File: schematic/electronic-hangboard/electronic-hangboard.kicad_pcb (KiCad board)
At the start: 2 copper layers, 74 x 45.3 mm, 40 parts, among them J1 UART, J2 Load cell, J3 JTAG, J4 Battery, Q1 2N7002, SW1 RESET, SW2 POWER_ON, U1 ESP32-WROOM-32, U2 HX711, U3 NCP1400A, U4 AMS1117-3.3

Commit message: Update pcb
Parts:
- removed C10: 68uF, Capacitor_SMD:C_1206_3216Metric_Pad1.33x1.80mm_HandSolder
- removed C9: 10uF, Capacitor_SMD:C_1206_3216Metric_Pad1.33x1.80mm_HandSolder
- removed H2, H3: MountingHole, MountingHole:MountingHole_3.2mm_M3
- removed L1: CR54−220MC - 22uH, Inductor_SMD:L_Bourns_SRP7028A_7.3x6.6mm
- removed SW1: RESET, Button_Switch_SMD:SW_Push_1P1T_NO_6x6mm_H9.5mm
- removed SW2: POWER_ON, Button_Switch_SMD:SW_Push_1P1T_NO_6x6mm_H9.5mm
- removed U3: NCP1400A, Package_TO_SOT_SMD:SOT-23-5_HandSoldering
- added C13: 4.7uF, Capacitor_SMD:C_1206_3216Metric_Pad1.33x1.80mm_HandSolder, F.Cu at (61.0, 65.2)
- added C14: 3.3pF, Capacitor_SMD:C_1206_3216Metric_Pad1.33x1.80mm_HandSolder, F.Cu at (49.5, 70.3)
- added C15: 4.7uF, Capacitor_SMD:C_1206_3216Metric_Pad1.33x1.80mm_HandSolder, F.Cu at (49.5, 65.2)
- added D2: MBR0520LT1, Diode_SMD:D_SOD-123, F.Cu at (49.8, 58.9)
- added D3: LED, Diode_SMD:D_1206_3216Metric_Pad1.42x1.75mm_HandSolder, F.Cu at (81.0, 36.1)
- added J5: UART, Connector_PinHeader_2.54mm:PinHeader_1x06_P2.54mm_Vertical, F.Cu at (34.3, 53.3)
- added J6: Conn_01x10_Pin, Connector_PinHeader_2.54mm:PinHeader_1x10_P2.54mm_Vertical, F.Cu at (72.6, 65.0)
- added L2: 10uH, Inductor_SMD:L_Bourns_SRP7028A_7.3x6.6mm, F.Cu at (57.1, 58.9)
- added R13: 200K, Resistor_SMD:R_1206_3216Metric_Pad1.30x1.75mm_HandSolder, F.Cu at (57.1, 67.8)
- added R14: 10K, Resistor_SMD:R_1206_3216Metric_Pad1.30x1.75mm_HandSolder, F.Cu at (59.4, 70.3)
- added R15: 330R, Resistor_SMD:R_1206_3216Metric_Pad1.30x1.75mm_HandSolder, F.Cu at (91.9, 36.1)
- added SW3: POWER_ON, Connector_PinHeader_2.54mm:PinHeader_1x02_P2.54mm_Vertical_SMD_Pin1Left, F.Cu at (66.0, 58.4)
- added U5: TPS61040DBV, Package_TO_SOT_SMD:SOT-23-5, F.Cu at (56.9, 64.5)
- D1: value MBR0520LT1 -> LED; footprint Diode_SMD:D_SOD-123 -> Diode_SMD:D_1206_3216Metric_Pad1.42x1.75mm_HandSolder
- H1: footprint MountingHole:MountingHole_3.2mm_M3 -> MountingHole:MountingHole_3.2mm_M3_DIN965_Pad_TopBottom
- J1: value UART -> BATTERY; footprint Connector_PinHeader_2.54mm:PinHeader_1x03_P2.54mm_Vertical -> Connector_PinHeader_2.54mm:PinHeader_1x02_P2.54mm_Vertical
- J2: value Load cell -> Conn_01x04_Pin; footprint Connector_Wire:SolderWire-0.1sqmm_1x04_P3.6mm_D0.4mm_OD1mm_Relief -> Connector_PinHeader_2.54mm:PinHeader_1x04_P2.54mm_Vertical
- J3: footprint Connector_PinHeader_2.54mm:PinHeader_1x07_P2.54mm_Vertical -> Connector_PinHeader_2.54mm:PinHeader_1x06_P2.54mm_Vertical
- J4: value Battery -> Conn_01x10_Pin; footprint Connector_Wire:SolderWire-0.1sqmm_1x02_P3.6mm_D0.4mm_OD1mm -> Connector_PinHeader_2.54mm:PinHeader_1x10_P2.54mm_Vertical
- Q1: value 2N7002 -> S9015
- R1: value R -> 10K
- R12: value 10K -> 330R
- R8: value 100R -> 620K
- R9: value 100R -> 1K2
- moved R8 131.4 mm to (49.5, 67.8), turned to 0 degrees
- moved U4 128.2 mm to (42.4, 60.3), turned to 90 degrees
- moved J1 126.9 mm to (34.3, 70.9), turned to 0 degrees
- moved C11 120.3 mm to (42.4, 67.5), turned to 90 degrees
- moved R2 110.8 mm to (38.9, 40.6)
- moved R3 110.8 mm to (38.8, 43.2)
- moved R5 110.7 mm to (38.8, 48.3)
- moved R4 110.7 mm to (38.9, 45.7)
- moved D1 110.2 mm to (75.4, 36.1), turned to 180 degrees
- moved R12 109.7 mm to (86.6, 36.1), turned to 180 degrees
- moved J3 108.5 mm to (34.3, 35.6)
- moved C3 105.4 mm to (37.8, 36.3)
- moved C6 103.7 mm to (91.8, 47.0)
- moved J2 103.4 mm to (95.6, 48.5), turned to 180 degrees
- moved R7 102.1 mm to (90.2, 41.6)
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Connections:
- C1 pad 2: GND -> E-
- C11 pad 1: GND -> E-
- C12 pad 2: GND -> E-
- C2 pad 2: GND -> E-
- C3 pad 1: GND -> E-
- C4 pad 2: GND -> E-
- C5 pad 1: GND -> E-
- C6 pad 1: GND -> E-
- C6 pad 2: Net-(J2-Pin_1) -> E+
- C7 pad 2: Net-(U2-INA-) -> S-
- D1 pad 1: +5V -> Net-(D1-K)
- D1 pad 2: Net-(D1-A) -> IO23
- J1 pad 1: TX -> E-
- J1 pad 2: RX -> +BATT
- J2 pad 1: Net-(J2-Pin_1) -> E+
- J2 pad 2: GND -> E-
- J2 pad 3: S- -> S+
- J2 pad 4: S+ -> S-
- J3 pad 2: GND -> E-
- J3 pad 3: EN -> Net-(J3-Pin_3)
- J3 pad 4: Net-(J3-TCK) -> Net-(J3-Pin_4)
- J3 pad 5: Net-(J3-TMS) -> Net-(J3-Pin_5)
- J3 pad 6: Net-(J3-TDO) -> Net-(J3-Pin_6)
- J4 pad 1: +BATT -> IO2
- J4 pad 2: GND -> SDI
- Q1 pad 1: Net-(Q1-G) -> E+
- Q1 pad 2: Net-(J2-Pin_1) -> Net-(Q1-B)
- R11 pad 2: GND -> E-
- R12 pad 1: CONV_EN -> E-
- R12 pad 2: GND -> Net-(D1-K)
- R2 pad 1: Net-(J3-TCK) -> Net-(J3-Pin_3)
- R3 pad 1: Net-(J3-TMS) -> Net-(J3-Pin_4)
- R4 pad 1: Net-(J3-TDO) -> Net-(J3-Pin_5)
- R5 pad 1: Net-(J3-TDI) -> Net-(J3-Pin_6)
- R6 pad 1: Net-(J2-Pin_1) -> E+
- R7 pad 2: GND -> E-
- R8 pad 1: S- -> +5V
- R8 pad 2: Net-(U2-INA-) -> Net-(U5-FB)
- U1 pad 1: GND -> E-
- U1 pad 10: unconnected-(U1-IO25-Pad10) -> IO25
- U1 pad 11: unconnected-(U1-IO26-Pad11) -> IO26
- U1 pad 12: unconnected-(U1-IO27-Pad12) -> IO27
- U1 pad 15: GND -> E-
- U1 pad 17: unconnected-(U1-SHD/SD2-Pad17) -> SHD
- U1 pad 18: unconnected-(U1-SWP/SD3-Pad18) -> SWP
- U1 pad 19: unconnected-(U1-SCS/CMD-Pad19) -> SCS
- U1 pad 20: unconnected-(U1-SCK/CLK-Pad20) -> SCK
- U1 pad 21: unconnected-(U1-SDO/SD0-Pad21) -> SDO
- U1 pad 22: unconnected-(U1-SDI/SD1-Pad22) -> SDI
- U1 pad 24: unconnected-(U1-IO2-Pad24) -> IO2
- U1 pad 25: Net-(SW1-A) -> RST
- U1 pad 31: SCK -> HX711_SCK
- U1 pad 33: unconnected-(U1-IO21-Pad33) -> IO21
- U1 pad 36: unconnected-(U1-IO22-Pad36) -> IO22
- U1 pad 37: unconnected-(U1-IO23-Pad37) -> IO23
- U1 pad 38: GND -> E-
- U1 pad 39: GND -> E-
- U1 pad 4: unconnected-(U1-SENSOR_VP-Pad4) -> VP
- U1 pad 5: unconnected-(U1-SENSOR_VN-Pad5) -> VN
- U1 pad 6: unconnected-(U1-IO34-Pad6) -> IO34
- U1 pad 7: unconnected-(U1-IO35-Pad7) -> IO35
- U1 pad 8: unconnected-(U1-IO32-Pad8) -> IO32
- U1 pad 9: unconnected-(U1-IO33-Pad9) -> IO33
- U2 pad 10: GND -> E-
- U2 pad 11: SCK -> HX711_SCK
- U2 pad 13: GND -> E-
- U2 pad 2: Net-(Q1-G) -> Net-(Q1-B)
- U2 pad 3: Net-(J2-Pin_1) -> E+
- U2 pad 5: GND -> E-
- U2 pad 7: Net-(U2-INA-) -> S-
- U2 pad 9: GND -> E-
- U4 pad 1: GND -> E-
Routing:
- net E-: track 0.00 -> 170.1 mm, vias 0 -> 2
- net GND: track 158.7 -> 0.00 mm
- net IO25: track 0.00 -> 79.6 mm, vias 0 -> 1
- net IO26: track 0.00 -> 76.3 mm, vias 0 -> 1
- net IO27: track 0.00 -> 73.9 mm, vias 0 -> 1
- net SHD: track 0.00 -> 67.7 mm, vias 0 -> 1
- net SWP: track 0.00 -> 63.4 mm, vias 0 -> 1
- net SCS: track 0.00 -> 60.0 mm, vias 0 -> 1
- net IO22: track 0.00 -> 55.6 mm, vias 0 -> 3
- net VP: track 0.00 -> 54.1 mm, vias 0 -> 1
- net VN: track 0.00 -> 54.0 mm, vias 0 -> 1
- net IO34: track 0.00 -> 53.6 mm, vias 0 -> 1
- net IO35: track 0.00 -> 53.4 mm, vias 0 -> 1
- net IO32: track 0.00 -> 52.2 mm, vias 0 -> 1
- net IO33: track 0.00 -> 52.0 mm, vias 0 -> 1
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- added copper zone on F.Cu, net +3V3
- added copper zone on F.Cu, net CONV_EN
- added copper zone on B.Cu, net E-
- added copper zone on F.Cu, net E-
- added copper zone on F.Cu, net Net-(D2-A)
- added copper zone on F.Cu, net Net-(U5-FB)
- removed copper zone on B.Cu, net GND
- removed copper zone on F.Cu, net Net-(D1-A)
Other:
- board size 74 x 45.3 mm -> 68.3 x 42.9 mm
- board text added: "2 DI DO CK CS WP HD 27 26 25"
- board text added: "33 32 35 34 VN VP 21 22 23 -"
- board text added: "3V3 GND CK MS DO DI"
- board text added: "3V3 GND RST EN TX RX"
- board text added: "CK MS DO DI"
- board text added: "GND BAT +"
- board text removed: "+"
- board text removed: "-"
- board text removed: "3V3"
- board text removed: "CK"
- board text removed: "DI"
- board text removed: "DO"
- board text removed: "EN"
- board text removed: "GND"
- board text removed: "MS"
- board text removed: "RX"
- board text removed: "TX"

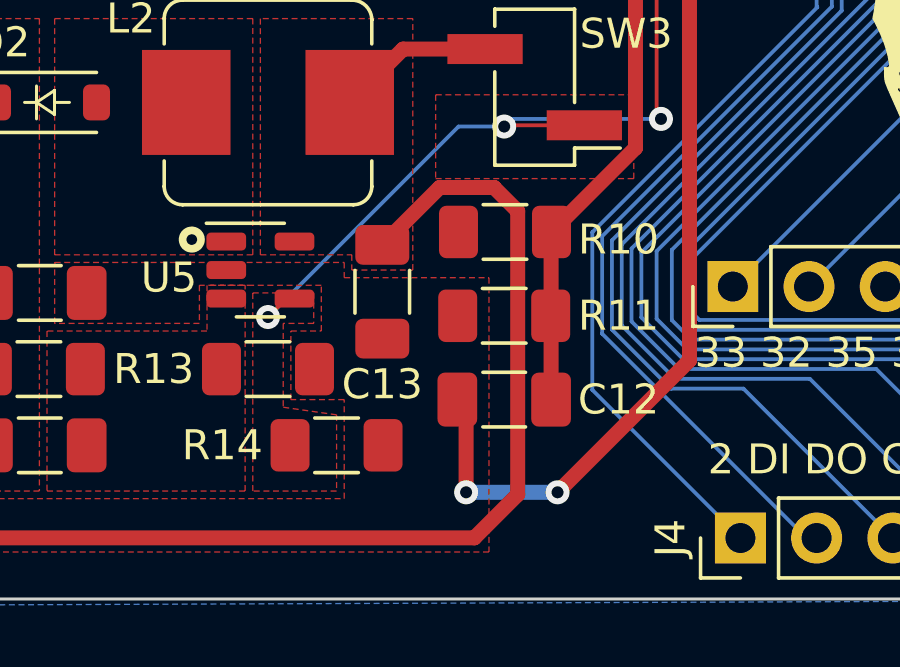
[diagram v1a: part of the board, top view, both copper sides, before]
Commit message: update schematic fix voltage divider not connected
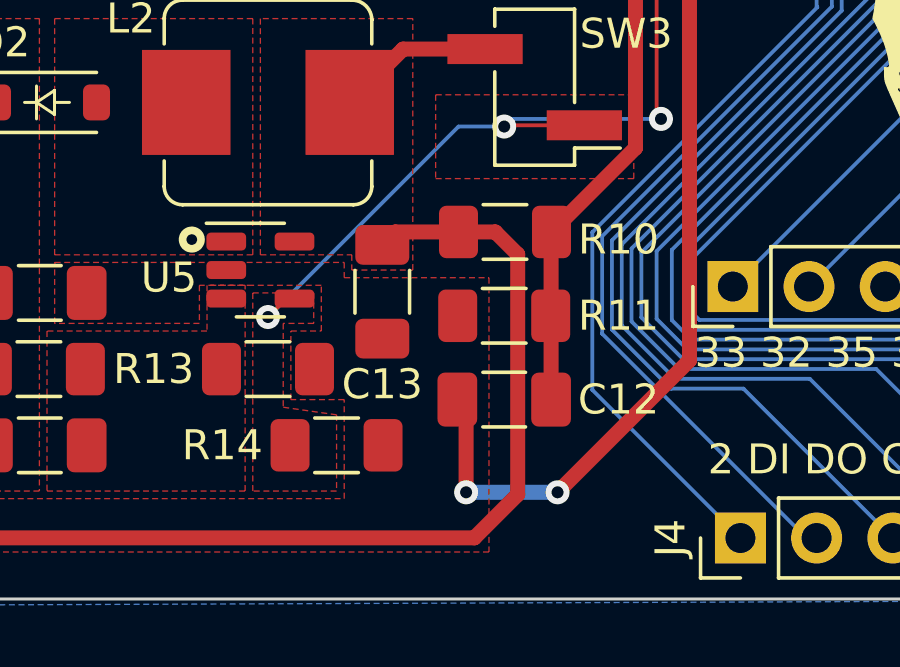
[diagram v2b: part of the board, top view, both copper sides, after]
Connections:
- R10 pad 1: VBAT -> +BATT
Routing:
- net +BATT: track 52.1 -> 50.0 mm
